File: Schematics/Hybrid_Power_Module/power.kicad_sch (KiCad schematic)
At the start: 93 parts, among them J1 ScrewSwitch, J2 Battery, J3 ScrewSwitch, J4 GSE, Q1 AO4447A, Q2 SI2305CDS, Q3 DMN6040SSD-13, U1 TPS61175PWPR, U10 LM66100DCKR, U11 LM66100DCKR, U12 AMS1117-3.3, U2 LM74700QDBVRQ1, U3 LM74700QDBVRQ1, U4 ACS37041KLHBLT-010B3, U5 ACS37041KLHBLT-010B5, U6 INA181A2, U7 LMR51430XDDCR, U8 LMR51430XDDCR, U9 LM66100DCKR

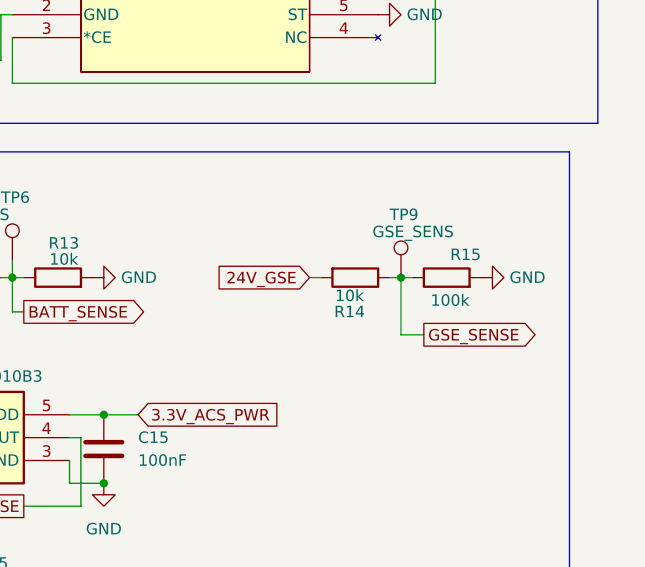
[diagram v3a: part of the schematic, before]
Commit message: fixed voltage divder for GSE 24v
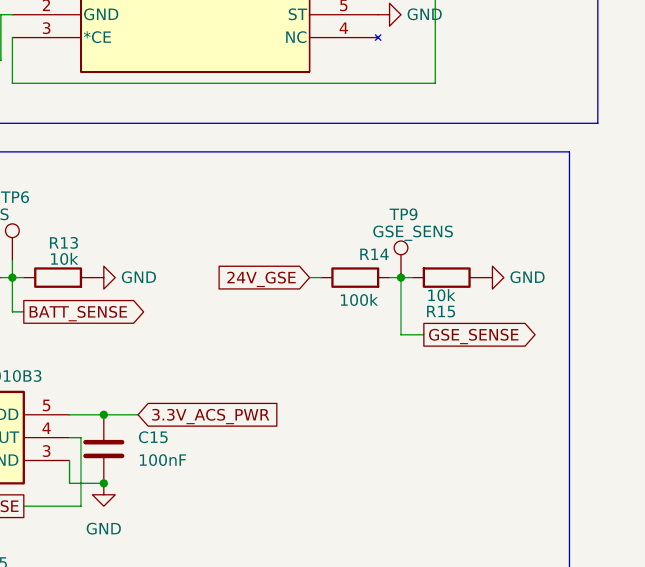
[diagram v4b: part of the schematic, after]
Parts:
- R14: value 10k -> 100k; LCSC C25804 -> C25803
- R15: value 100k -> 10k; LCSC C25803 -> C25804
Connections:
- net 24V_GSE: now also R14.1; no longer R14.2
- net GND: now also R15.1; no longer R15.2
- net GSE_SENSE: now also R14.2, R15.2; no longer R14.1, R15.1
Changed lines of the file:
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@@
 			)
 		)
-		(property "Description" "Shunt Resistor"
+		(property "Description" "SHUNT"
 			(at 308.61 208.28 0)
 			(effects
@@
 	)
 	(symbol
+		(lib_id "Device:R")
+		(at 379.73 135.89 90)
+		(unit 1)
+		(exclude_from_sim no)
+		(in_bom yes)
+		(on_board yes)
+		(dnp no)
+		(property "Reference" "R14"
+			(at 383.54 133.35 90)
+			(effects
+				(font
+					(size 1.27 1.27)
+				)
+				(justify left)
+			)
+		)
+		(property "Value" "100k"
+			(at 382.27 138.43 90)
+			(effects
+				(font
+					(size 1.27 1.27)
+				)
+				(justify left)
+			)
+		)
+		(property "Footprint" "Resistor_SMD:R_0603_1608Metric"
+			(at 379.73 137.668 90)
+			(effects
+				(font
+					(size 1.27 1.27)
+				)
+				(hide yes)
+			)
+		)
+		(property "Datasheet" "~"
+			(at 379.73 135.89 0)
+			(effects
+				(font
+					(size 1.27 1.27)
+				)
+				(hide yes)
+			)
+		)
+		(property "Description" "Resistor"
+			(at 379.73 135.89 0)
+			(effects
+				(font
+					(size 1.27 1.27)
+				)
+				(hide yes)
+			)
+		)
+		(property "LCSC" "C25803"
+			(at 379.73 135.89 0)
+			(effects
+				(font
+					(size 1.27 1.27)
+				)
+				(hide yes)
+			)
+		)
+		(pin "2"
+		)
+		(pin "1"
+		)
+		(instances
+			(project "Power_Module"
+				(path "/11b1f19b-ce82-4fce-baf6-0357ef2e3f24/f4c51f51-72e5-4abd-a0d4-d966d9c5494e"
+					(reference "R14")
+					(unit 1)
+				)
+			)
+		)
+	)
+	(symbol
 		(lib_id "Device:C")
 		(at 355.6 212.09 0)
@@
 	)
 	(symbol
+		(lib_id "Device:R")
+		(at 389.89 135.89 270)
+		(unit 1)
+		(exclude_from_sim no)
+		(in_bom yes)
+		(on_board yes)
+		(dnp no)
+		(property "Reference" "R15"
+			(at 389.255 139.7 90)
+			(effects
+				(font
+					(size 1.27 1.27)
+				)
+			)
+		)
+		(property "Value" "10k"
+			(at 389.255 137.9108 90)
+			(effects
+				(font
+					(size 1.27 1.27)
+				)
+			)
+		)
+		(property "Footprint" "Resistor_SMD:R_0603_1608Metric"
+			(at 389.89 134.112 90)
+			(effects
+				(font
+					(size 1.27 1.27)
+				)
+				(hide yes)
+			)
+		)
+		(property "Datasheet" "~"
+			(at 389.89 135.89 0)
+			(effects
+				(font
+					(size 1.27 1.27)
+				)
+				(hide yes)
+			)
+		)
+		(property "Description" ""
+			(at 389.89 135.89 0)
+			(effects
+				(font
+					(size 1.27 1.27)
+				)
+				(hide yes)
+			)
+		)
+		(property "LCSC" "C25804"
+			(at 389.89 135.89 0)
+			(effects
+				(font
+					(size 1.27 1.27)
+				)
+				(hide yes)
+			)
+		)
+		(pin "1"
+		)
+		(pin "2"
+		)
+		(instances
+			(project "Power_Module"
+				(path "/11b1f19b-ce82-4fce-baf6-0357ef2e3f24/f4c51f51-72e5-4abd-a0d4-d966d9c5494e"
+					(reference "R15")
+					(unit 1)
+				)
+			)
+		)
+	)
+	(symbol
 		(lib_id "Device:C")
 		(at 76.2 198.12 0)
@@
 	)
 	(symbol
-		(lib_id "Device:R")
-		(at 389.89 135.89 90)
-		(unit 1)
-		(exclude_from_sim no)
-		(in_bom yes)
-		(on_board yes)
-		(dnp no)
-		(property "Reference" "R15"
-			(at 393.7 133.35 90)
-			(effects
-				(font
-					(size 1.27 1.27)
-				)
-				(justify left)
-			)
-		)
-		(property "Value" "100k"
-			(at 392.43 138.43 90)
-			(effects
-				(font
-					(size 1.27 1.27)
-				)
-				(justify left)
-			)
-		)
-		(property "Footprint" "Resistor_SMD:R_0603_1608Metric"
-			(at 389.89 137.668 90)
-			(effects
-				(font
-					(size 1.27 1.27)
-				)
-				(hide yes)
-			)
-		)
-		(property "Datasheet" "~"
-			(at 389.89 135.89 0)
-			(effects
-				(font
-					(size 1.27 1.27)
-				)
-				(hide yes)
-			)
-		)
-		(property "Description" "Resistor"
-			(at 389.89 135.89 0)
-			(effects
-				(font
-					(size 1.27 1.27)
-				)
-				(hide yes)
-			)
-		)
-		(property "LCSC" "C25803"
-			(at 389.89 135.89 0)
-			(effects
-				(font
-					(size 1.27 1.27)
-				)
-				(hide yes)
-			)
-		)
-		(pin "2"
-		)
-		(pin "1"
-		)
-		(instances
-			(project ""
-				(path "/11b1f19b-ce82-4fce-baf6-0357ef2e3f24/f4c51f51-72e5-4abd-a0d4-d966d9c5494e"
-					(reference "R15")
-					(unit 1)
-				)
-			)
-		)
-	)
-	(symbol
 		(lib_id "Device:C")
 		(at 93.98 36.83 0)
@@
 					(unit 1)
 				)
-			)
-		)
-	)
-	(symbol
-		(lib_id "Device:R")
-		(at 379.73 135.89 270)
-		(unit 1)
-		(exclude_from_sim no)
-		(in_bom yes)
-		(on_board yes)
-		(dnp no)
-		(property "Reference" "R14"
-			(at 379.095 139.7 90)
-			(effects
-				(font
-					(size 1.27 1.27)
-				)
-			)
-		)
-		(property "Value" "10k"
-			(at 379.095 137.9108 90)
-			(effects
-				(font
-					(size 1.27 1.27)
-				)
-			)
-		)
-		(property "Footprint" "Resistor_SMD:R_0603_1608Metric"
-			(at 379.73 134.112 90)
-			(effects
-				(font
-					(size 1.27 1.27)
-				)
-				(hide yes)
-			)
-		)
-		(property "Datasheet" "~"
-			(at 379.73 135.89 0)
-			(effects
-				(font
-					(size 1.27 1.27)
-				)
-				(hide yes)
-			)
-		)
-		(property "Description" ""
-			(at 379.73 135.89 0)
-			(effects
-				(font
-					(size 1.27 1.27)
-				)
-				(hide yes)
-			)
-		)
-		(property "LCSC" "C25804"
-			(at 379.73 135.89 0)
-			(effects
-				(font
-					(size 1.27 1.27)
-				)
-				(hide yes)
-			)
-		)
-		(pin "1"
-		)
-		(pin "2"
-		)
-		(instances
-			(project "Power_Module"
-				(path "/11b1f19b-ce82-4fce-baf6-0357ef2e3f24/f4c51f51-72e5-4abd-a0d4-d966d9c5494e"
-					(reference "R14")
-					(unit 1)
-				)

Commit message: changed current sense and switched to bidirectional TVS for GSE power
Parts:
- removed D1, D2: SMAJ30A, Diode_SMD:D_SMA, symbol Diode:SMAJ30A
- added C49, C50, C52, C53: 22uF, Capacitor_SMD:C_1206_3216Metric, symbol Device:C
- added D9: SMAJ30CA, Diode_SMD:D_SMA, symbol Diode:SMAJ30CA
- added J7: Stack Male Edge Connector, Connector_PCBEdge:BUS_PCIexpress_x1, symbol EdgeConnectorV2:Stack Male Edge Connector
- U6: value INA181A2 -> INA187A; Digikey (none) -> 296-INA187A1IDBVRCT-ND; LCSC C192764 -> (none)
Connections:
- net 24V_MUX: now also C50.1, J7.A17 (24V_A), J7.A18 (24V_A)
- net 3.3V_PSU: now also C53.1, J7.A1 (3.3V_A), J7.A2 (3.3V_A)
- net GND: now also C49.2, C50.2, C52.2, C53.2, D9.1 (A1), J7.A3 (GND_A), J7.A6 (GND_A), J7.B4 (GND_A), J7.B5 (GND_A), J7.B6 (GND_A)
- net GSE_SW+: now also D9.2 (A2)
- net V_BATT: now also C52.1, J7.B1 (BATT_A), J7.B2 (BATT_A), J7.B3 (BATT_A)
- net 5V_PSU renamed 5.0V_A
- net 5.0V_A: now also C49.1, J7.A4 (5.0V_A), J7.A5 (5.0V_A)
- new net: J7.A12 (GND_B), J7.A9 (GND_B), J7.B10 (GND_B), J7.B11 (GND_B), J7.B12 (GND_B)
- new net: J7.A7 (3.3V_B), J7.A8 (3.3V_B)
- new net: J7.B7 (BATT_B), J7.B8 (BATT_B), J7.B9 (BATT_B)
- new net CAN_N: J7.B14 (CAN_H)
- new net CAN_P: J7.B13 (CAN_L)
- no-connect marks 0 -> 4
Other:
- note added: "Edge Connector"
- moved on the sheet: C13, C14, C15, C16, C17, R11, R12, R13, R14, R15, R5, R6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

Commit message: final board submitted to cart
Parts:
- C49, C52, C53: Digikey 445-8045-1-ND -> (none); LCSC (none) -> C12891
- TP1: value BATT_GND1 -> GND
- TP13: value GSEV -> 24V.G
- TP2: value GSE_GND1 -> GND
- TP3: value 24V_PSU -> 24V.B
- TP4: value 24V_MUX -> 24V.OR
- TP5: value 5VSENS -> 5V.S
- TP6: value A.S -> B.S
- TP9: value GSE_SENS -> GSE.S
- U1: Digikey (none) -> 296-24013-1-ND; LCSC C43276 -> (none)
- U7, U8: Digikey (none) -> 296-LMR51430XDDCRCT-ND; LCSC C5185863 -> (none); _Digikey 296-LMR51430XDDCRCT-ND -> (none)
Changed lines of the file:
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@@
 			)
 		)
-		(property "Value" "24V_PSU"
+		(property "Value" "24V.B"
 			(at 96.52 30.9879 0)
 			(effects
@@
 			)
 		)
-		(property "Description" ""
+		(property "Description" "24V.B"
 			(at 93.98 33.02 0)
 			(effects
@@
 			)
 		)
-		(property "Value" "GSE_SENS"
+		(property "Value" "GSE.S"
 			(at 297.815 97.79 0)
 			(effects
@@
 			)
 		)
-		(property "Description" ""
+		(property "Description" "GSE.S"
 			(at 300.99 102.87 0)
 			(effects
@@
 			)
 		)
-		(property "Value" "A.S"
+		(property "Value" "B.S"
 			(at 254.635 95.885 0)
 			(effects
@@
 			)
 		)
-		(property "Description" ""
+		(property "Description" "B.S"
 			(at 257.81 100.965 0)
 			(effects
@@
 			)
 		)
-		(property "_Digikey" "296-LMR51430XDDCRCT-ND"
-			(at 256.54 29.21 0)
-			(effects
-				(font
-					(size 1.27 1.27)
-				)
-				(hide yes)
-			)
-		)
-		(property "LCSC" "C5185863"
+		(property "Digikey" "296-LMR51430XDDCRCT-ND"
 			(at 256.54 29.21 0)
 			(effects
@@
 			)
 		)
-		(property "_Digikey" "296-LMR51430XDDCRCT-ND"
-			(at 256.54 67.31 0)
-			(effects
-				(font
-					(size 1.27 1.27)
-				)
-				(hide yes)
-			)
-		)
-		(property "LCSC" "C5185863"
+		(property "Digikey" "296-LMR51430XDDCRCT-ND"
 			(at 256.54 67.31 0)
 			(effects
@@
 			)
 		)
-		(property "Value" "5VSENS"
+		(property "Value" "5V.S"
 			(at 219.075 97.155 0)
 			(effects
@@
 			)
 		)
-		(property "Description" ""
+		(property "Description" "5V.S"
 			(at 222.25 102.235 0)
 			(effects
@@
 			)
 		)
-		(property "LCSC" "C43276"
+		(property "Digikey" "296-24013-1-ND"
 			(at 58.42 44.45 0)
 			(effects
@@
 			)
 		)
-		(property "Value" "BATT_GND1"
+		(property "Value" "GND"
 			(at 62.23 135.89 90)
 			(effects
@@
 			)
 		)
-		(property "Description" ""
+		(property "Description" "GND"
 			(at 58.42 133.35 0)
 			(effects
@@
 			)
 		)
-		(property "Description" ""
+		(property "Description" "3v3"
 			(at 236.22 120.65 0)
 			(effects
@@
 			)
 		)
-		(property "Description" ""
+		(property "Description" "5V"
 			(at 236.22 140.97 0)
 			(effects
@@
 			)
 		)
-		(property "Digikey" "445-8045-1-ND"
+		(property "LCSC" " C12891"
 			(at 269.24 243.84 0)
 			(effects
@@
 			)
 		)
-		(property "Value" "GSE_GND1"
+		(property "Value" "GND"
 			(at 67.31 267.4619 0)
 			(effects
@@
 			)
 		)
-		(property "Description" ""
+		(property "Description" "GND"
 			(at 64.77 262.89 0)
 			(effects
@@
 			)
 		)
-		(property "Digikey" "445-8045-1-ND"
+		(property "LCSC" " C12891"
 			(at 264.16 220.98 0)
 			(effects
@@
 			)
 		)
-		(property "Digikey" "445-8045-1-ND"
+		(property "LCSC" "C12891"
 			(at 269.24 224.79 0)
 			(effects
@@
 			)
 		)
-		(property "Value" "GSEV"
+		(property "Value" "24V.G"
 			(at 69.215 242.57 0)
 			(effects
@@
 			)
 		)
-		(property "Description" ""
+		(property "Description" "24V.G"
 			(at 72.39 247.65 0)
 			(effects
@@
 			)
 		)
-		(property "Value" "24V_MUX"
+		(property "Value" "24V.OR"
 			(at 223.52 184.9119 0)
 			(effects
@@
 			)
 		)
-		(property "Description" ""
+		(property "Description" "24V"
 			(at 220.98 180.34 0)
 			(effects
@@
 			)
 		)
-		(property "Description" ""
+		(property "Description" "BATT"
 			(at 67.31 125.73 0)
 			(effects
